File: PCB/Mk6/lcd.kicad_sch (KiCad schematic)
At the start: 2 parts

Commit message: save
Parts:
- added JP7: FontSize, Connector_PinHeader_2.54mm:PinHeader_1x03_P2.54mm_Vertical, symbol Jumper:Jumper_3_Open
- renumbered LCD1 to LCD2, RV1 to RV2
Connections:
- net +5V: now also JP7.3 (B)
- net GND: now also JP7.1 (A); no longer LCD2.1 (FG)
- new net: JP7.2 (C), LCD2.1 (FG)
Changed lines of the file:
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@@
+	)
+	(junction
+		(at 21.59 38.1)
+		(diameter 0)
+		(color 0 0 0 0)
+	)
+	(junction
+		(at 85.09 25.4)
+		(diameter 0)
+		(color 0 0 0 0)
 	)
 	(junction
@@
 	)
 	(junction
-		(at 29.21 33.02)
-		(diameter 0)
-		(color 0 0 0 0)
-	)
-	(junction
 		(at 85.09 33.02)
 		(diameter 0)
@@
 	(wire
 		(pts
-			(xy 29.21 22.86) (xy 29.21 33.02)
-		)
-		(stroke
-			(width 0)
-			(type default)
-		)
-	)
-	(wire
-		(pts
 			(xy 49.53 31.75) (xy 49.53 36.83)
 		)
@@
 	(wire
 		(pts
-			(xy 21.59 33.02) (xy 21.59 44.45)
-		)
-		(stroke
-			(width 0)
-			(type default)
-		)
-	)
-	(wire
-		(pts
-			(xy 85.09 19.05) (xy 85.09 33.02)
+			(xy 85.09 25.4) (xy 85.09 33.02)
+		)
+		(stroke
+			(width 0)
+			(type default)
+		)
+	)
+	(wire
+		(pts
+			(xy 29.21 31.75) (xy 31.75 31.75)
+		)
+		(stroke
+			(width 0)
+			(type default)
+		)
+	)
+	(wire
+		(pts
+			(xy 21.59 38.1) (xy 21.59 44.45)
+		)
+		(stroke
+			(width 0)
+			(type default)
+		)
+	)
+	(wire
+		(pts
+			(xy 21.59 22.86) (xy 21.59 38.1)
+		)
+		(stroke
+			(width 0)
+			(type default)
+		)
+	)
+	(wire
+		(pts
+			(xy 25.4 25.4) (xy 85.09 25.4)
+		)
+		(stroke
+			(width 0)
+			(type default)
+		)
+	)
+	(wire
+		(pts
+			(xy 85.09 19.05) (xy 85.09 25.4)
+		)
+		(stroke
+			(width 0)
+			(type default)
+		)
+	)
+	(wire
+		(pts
+			(xy 99.06 21.59) (xy 99.06 25.4)
+		)
+		(stroke
+			(width 0)
+			(type default)
+		)
+	)
+	(wire
+		(pts
+			(xy 21.59 38.1) (xy 25.4 38.1)
 		)
 		(stroke
@@
 	(wire
 		(pts
+			(xy 77.47 22.86) (xy 77.47 36.83)
+		)
+		(stroke
+			(width 0)
+			(type default)
+		)
+	)
+	(wire
+		(pts
 			(xy 52.07 31.75) (xy 52.07 36.83)
 		)
@@
 	(wire
 		(pts
-			(xy 29.21 22.86) (xy 77.47 22.86)
+			(xy 21.59 22.86) (xy 77.47 22.86)
 		)
 		(stroke
@@
 	(wire
 		(pts
-			(xy 77.47 22.86) (xy 77.47 36.83)
-		)
-		(stroke
-			(width 0)
-			(type default)
-		)
-	)
-	(wire
-		(pts
-			(xy 57.15 31.75) (xy 57.15 36.83)
+			(xy 57.15 20.32) (xy 57.15 36.83)
 		)
 		(stroke
@@
 	(wire
 		(pts
-			(xy 29.21 33.02) (xy 31.75 33.02)
-		)
-		(stroke
-			(width 0)
-			(type default)
-		)
-	)
-	(wire
-		(pts
 			(xy 85.09 33.02) (xy 85.09 35.56)
 		)
@@
 	(wire
 		(pts
-			(xy 72.39 25.4) (xy 72.39 36.83)
-		)
-		(stroke
-			(width 0)
-			(type default)
-		)
-	)
-	(wire
-		(pts
-			(xy 99.06 25.4) (xy 72.39 25.4)
-		)
-		(stroke
-			(width 0)
-			(type default)
-		)
-	)
-	(wire
-		(pts
-			(xy 21.59 33.02) (xy 29.21 33.02)
+			(xy 72.39 21.59) (xy 72.39 36.83)
+		)
+		(stroke
+			(width 0)
+			(type default)
+		)
+	)
+	(wire
+		(pts
+			(xy 99.06 21.59) (xy 72.39 21.59)
 		)
 		(stroke
@@
 	(wire
 		(pts
-			(xy 31.75 33.02) (xy 31.75 36.83)
-		)
-		(stroke
-			(width 0)
-			(type default)
-		)
-	)
-	(wire
-		(pts
 			(xy 85.09 35.56) (xy 85.09 36.83)
 		)
@@
 	(wire
 		(pts
+			(xy 31.75 31.75) (xy 31.75 36.83)
+		)
+		(stroke
+			(width 0)
+			(type default)
+		)
+	)
+	(wire
+		(pts
 			(xy 80.01 33.02) (xy 80.01 36.83)
 		)
@@
 	(global_label "DISP"
 		(shape input)
-		(at 57.15 31.75 90)
-		(fields_autoplaced yes)
-		(effects
-			(font
-				(size 1.27 1.27)
-			)
-			(justify left)
-		)
-		(property "Intersheetrefs" "${INTERSHEET_REFS}"
-			(at 57.15 24.4105 90)
+		(at 57.15 20.32 90)
+		(fields_autoplaced yes)
+		(effects
+			(font
+				(size 1.27 1.27)
+			)
+			(justify left)
+		)
+		(property "Intersheetrefs" "${INTERSHEET_REFS}"
+			(at 57.15 12.9805 90)
 			(effects
 				(font
@@
 		(on_board yes)
 		(dnp no)
-		(property "Reference" "RV1"
+		(property "Reference" "RV2"
 			(at 96.52 23.622 0)
 			(effects
@@
 			(project "Mk6"
 				(path "/d41350ce-2040-418d-ae11-f076a5474776/4c5e0103-ac1e-400b-b6d0-d77307a1336e"
-					(reference "RV1")
+					(reference "RV2")
 					(unit 1)
 				)
@@
 		(dnp no)
 		(fields_autoplaced yes)
-		(property "Reference" "#PWR03"
+		(property "Reference" "#PWR038"
 			(at 85.09 22.86 0)
 			(effects
@@
 			(project "Mk6"
 				(path "/d41350ce-2040-418d-ae11-f076a5474776/4c5e0103-ac1e-400b-b6d0-d77307a1336e"
-					(reference "#PWR03")
+					(reference "#PWR038")
+					(unit 1)
+				)
+			)
+		)
+	)
+	(symbol
+		(lib_id "Jumper:Jumper_3_Open")
+		(at 25.4 31.75 90)
+		(unit 1)
+		(exclude_from_sim no)
+		(in_bom no)
+		(on_board yes)
+		(dnp no)
+		(property "Reference" "JP7"
+			(at 28.448 35.306 0)
+			(effects
+				(font
+					(size 1.27 1.27)
+				)
+			)
+		)
+		(property "Value" "FontSize"
+			(at 19.304 31.75 0)
+			(effects
+				(font
+					(size 1.27 1.27)
+				)
+			)
+		)
+		(property "Footprint" "Connector_PinHeader_2.54mm:PinHeader_1x03_P2.54mm_Vertical"
+			(at 25.4 31.75 0)
+			(effects
+				(font
+					(size 1.27 1.27)
+				)
+				(hide yes)
+			)
+		)
+		(property "Datasheet" "~"
+			(at 25.4 31.75 0)
+			(effects
+				(font
+					(size 1.27 1.27)
+				)
+				(hide yes)
+			)
+		)
+		(property "Description" "Jumper, 3-pole, both open"
+			(at 25.4 31.75 0)
+			(effects
+				(font
+					(size 1.27 1.27)
+				)
+				(hide yes)
+			)
+		)
+		(pin "3"
+		)
+		(pin "2"
+		)
+		(pin "1"
+		)
+		(instances
+			(project "Mk6"
+				(path "/d41350ce-2040-418d-ae11-f076a5474776/4c5e0103-ac1e-400b-b6d0-d77307a1336e"
+					(reference "JP7")
 					(unit 1)
 				)
@@
 		(dnp no)
 		(fields_autoplaced yes)
-		(property "Reference" "#PWR014"
+		(property "Reference" "#PWR039"
 			(at 21.59 53.34 0)
 			(effects
@@
 			(project "Mk6"
 				(path "/d41350ce-2040-418d-ae11-f076a5474776/4c5e0103-ac1e-400b-b6d0-d77307a1336e"
-					(reference "#PWR014")
+					(reference "#PWR039")
 					(unit 1)
 				)
@@
 		(on_board yes)
 		(dnp no)
-		(property "Reference" "LCD1"
+		(property "Reference" "LCD2"
 			(at 93.98 49.53 0)
 			(effects
@@
 			(project "Mk6"
 				(path "/d41350ce-2040-418d-ae11-f076a5474776/4c5e0103-ac1e-400b-b6d0-d77307a1336e"
-					(reference "LCD1")
+					(reference "LCD2")
 					(unit 1)
 				)

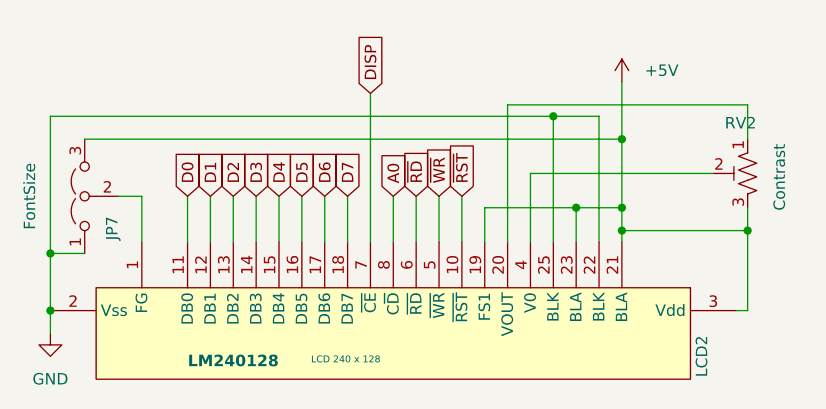
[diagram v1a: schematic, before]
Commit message: all done, pre-clk div
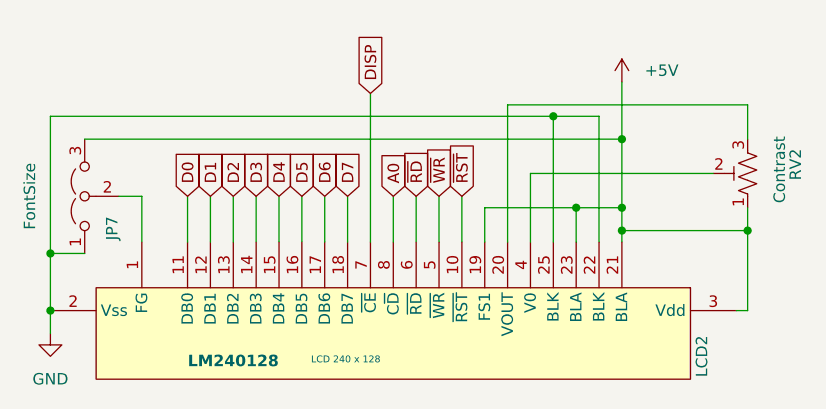
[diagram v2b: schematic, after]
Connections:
- net +5V: now also RV2.1; no longer RV2.3
- net at LCD2.20 (VOUT): now also RV2.3; no longer RV2.1
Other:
- moved on the sheet: RV2
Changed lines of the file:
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@@
 	(symbol
 		(lib_id "RetroParts_Library:R_Trim")
-		(at 99.06 29.21 0)
-		(mirror y)
+		(at 99.06 29.21 180)
 		(unit 1)
 		(exclude_from_sim no)
@@
 		(dnp no)
 		(property "Reference" "RV2"
-			(at 96.52 23.622 0)
+			(at 104.394 29.972 90)
 			(effects
 				(font
@@
 		)
 		(property "Value" "Contrast"
-			(at 102.616 25.908 90)
+			(at 102.616 32.512 90)
 			(effects
 				(font

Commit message: Added 3-8 IO, extra GAL out, attachment point for !RAM
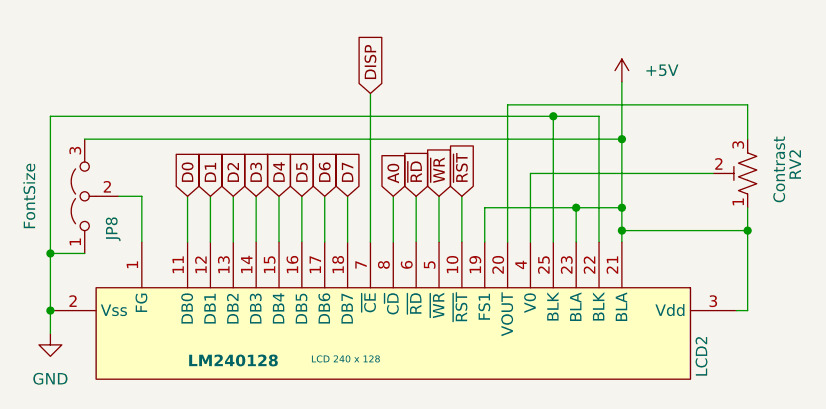
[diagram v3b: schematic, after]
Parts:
- renumbered JP7 to JP8
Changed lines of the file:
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@@
 		(dnp no)
 		(fields_autoplaced yes)
-		(property "Reference" "#PWR038"
+		(property "Reference" "#PWR039"
 			(at 85.09 22.86 0)
 			(effects
@@
 			(project "Mk6"
 				(path "/d41350ce-2040-418d-ae11-f076a5474776/4c5e0103-ac1e-400b-b6d0-d77307a1336e"
-					(reference "#PWR038")
+					(reference "#PWR039")
 					(unit 1)
 				)
@@
 		(on_board yes)
 		(dnp no)
-		(property "Reference" "JP7"
+		(property "Reference" "JP8"
 			(at 28.448 35.306 0)
 			(effects
@@
 			(project "Mk6"
 				(path "/d41350ce-2040-418d-ae11-f076a5474776/4c5e0103-ac1e-400b-b6d0-d77307a1336e"
-					(reference "JP7")
+					(reference "JP8")
 					(unit 1)
 				)
@@
 		(dnp no)
 		(fields_autoplaced yes)
-		(property "Reference" "#PWR039"
+		(property "Reference" "#PWR040"
 			(at 21.59 53.34 0)
 			(effects
@@
 			(project "Mk6"
 				(path "/d41350ce-2040-418d-ae11-f076a5474776/4c5e0103-ac1e-400b-b6d0-d77307a1336e"
-					(reference "#PWR039")
+					(reference "#PWR040")
 					(unit 1)
 				)
